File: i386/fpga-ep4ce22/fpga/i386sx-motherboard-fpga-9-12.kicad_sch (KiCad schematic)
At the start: 15 parts, among them J3 JTAG, J4 SPI ISP, J5 UART, U2 SN74AHCT1G125DBVR, U3 (3/6) EP4CE22F17C8N, U5 W25Q128JVSIQ

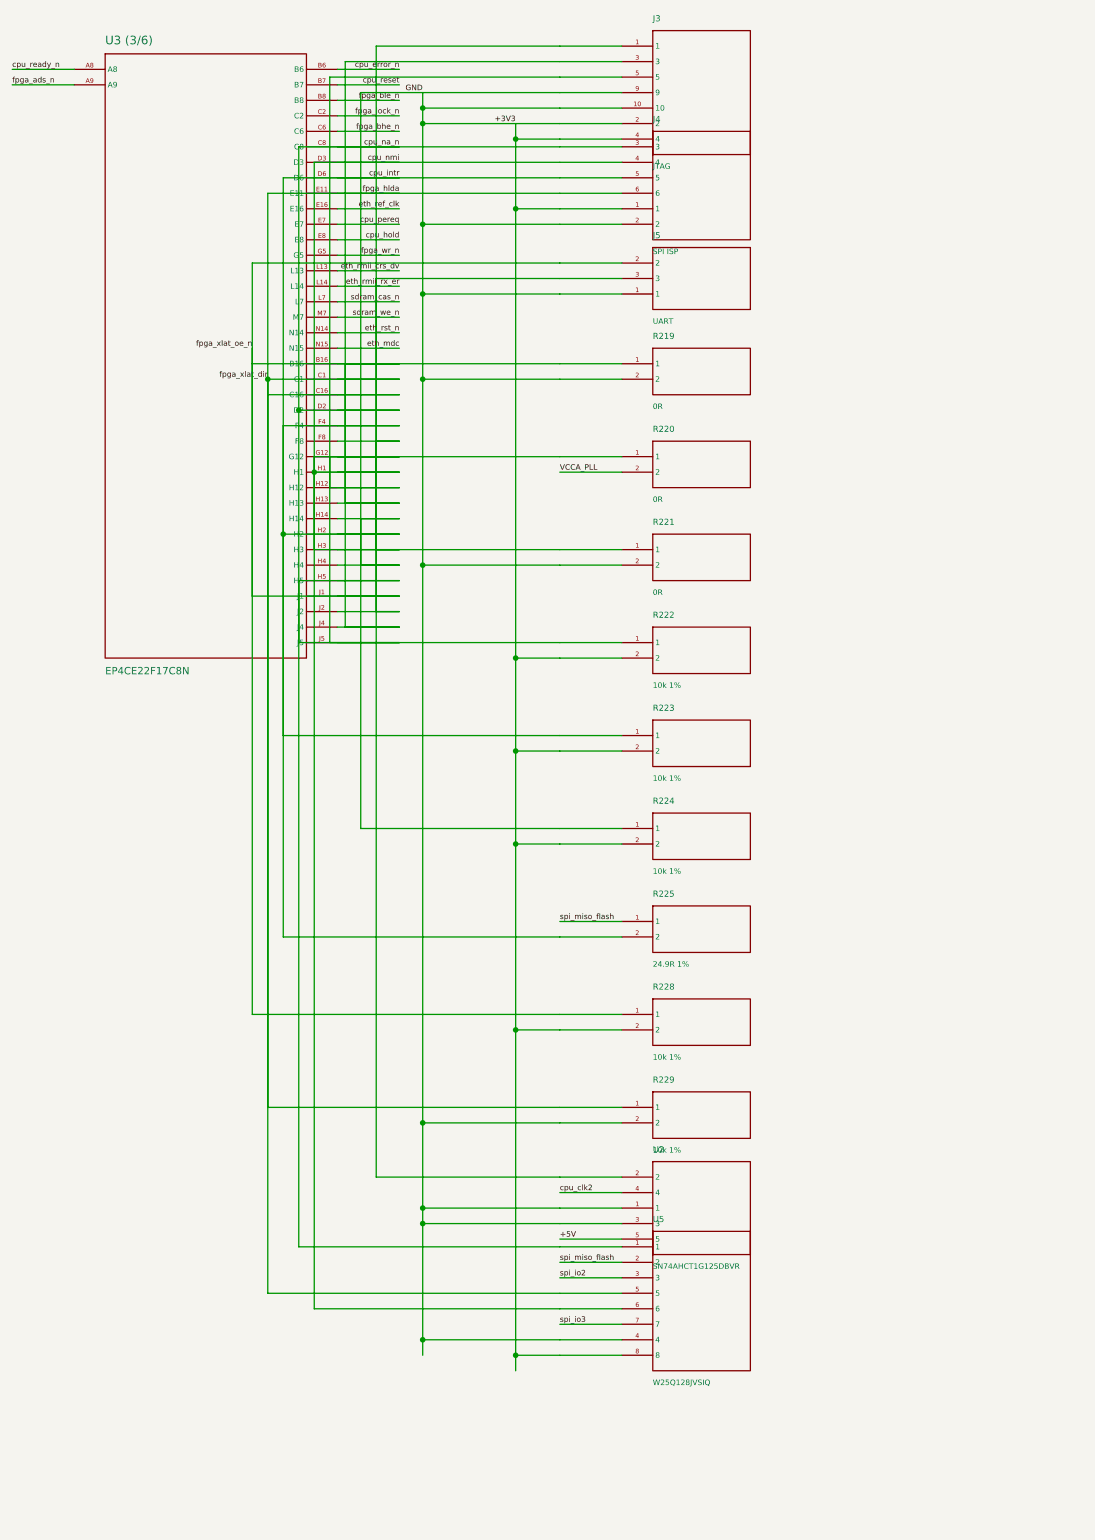
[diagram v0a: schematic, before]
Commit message: Publish the motherboards' KiCad files
From socket3@c0f6464 socket7@9205469 socket370@524f5b1 i386@bea926c
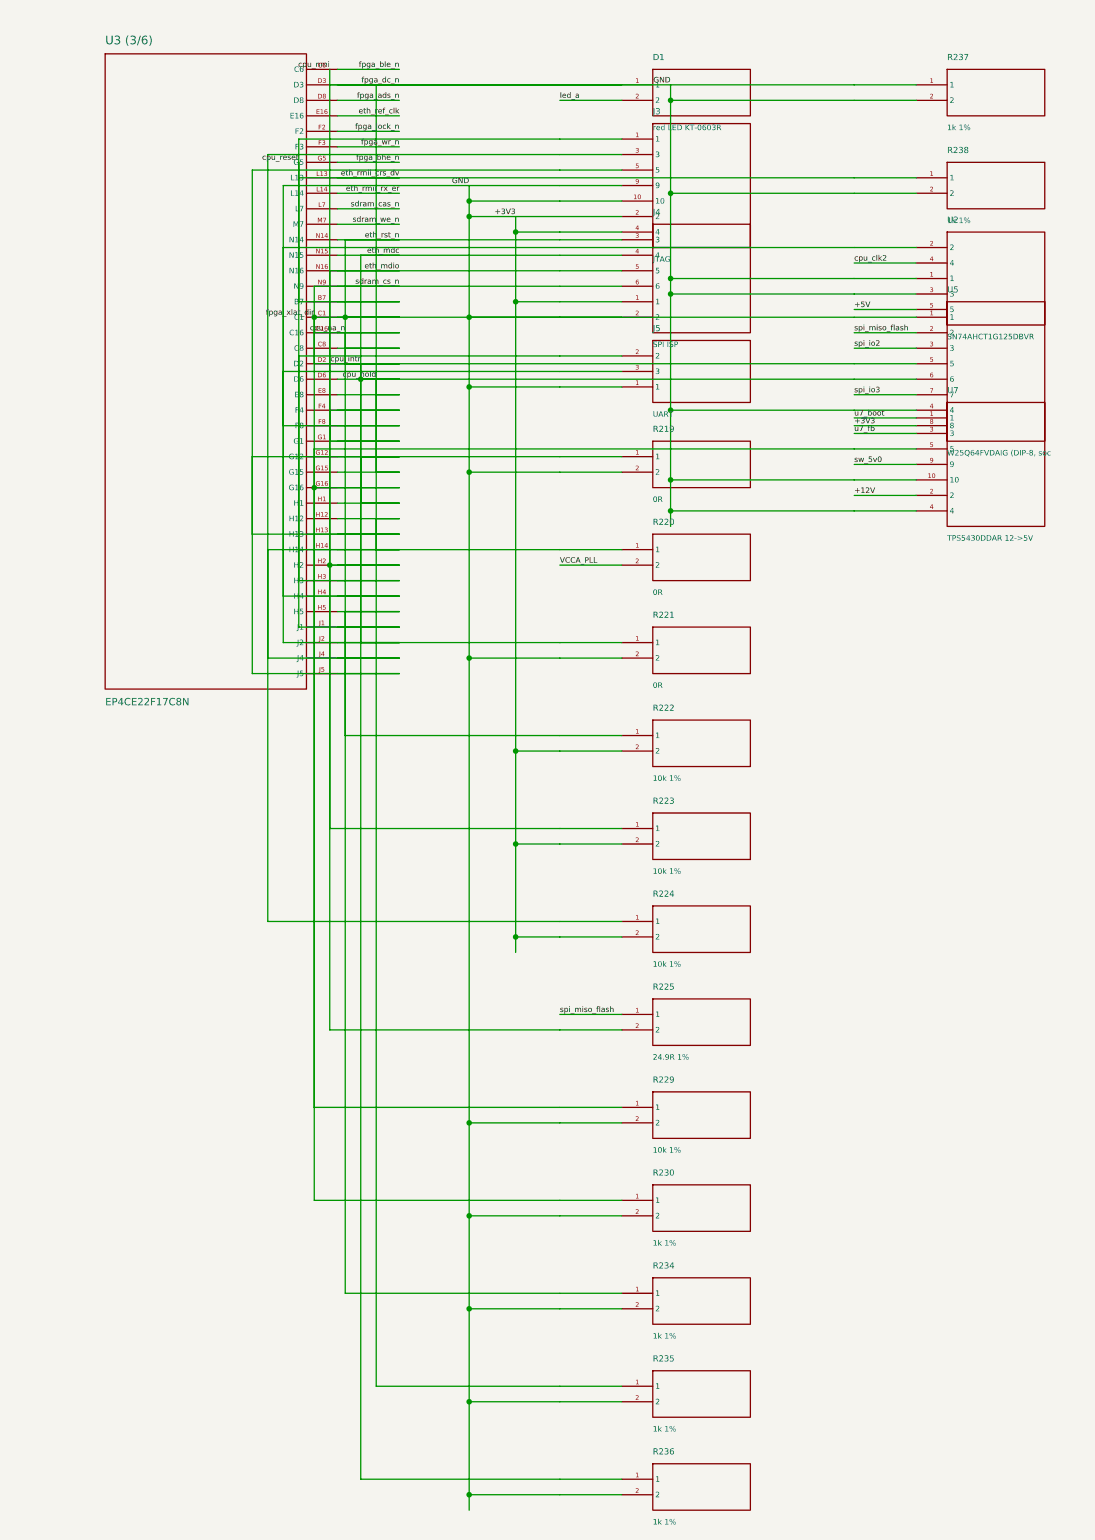
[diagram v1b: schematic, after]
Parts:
- removed R228: 10k 1%, symbol gen:S2_0s
- removed U3 (3/6): EP4CE22F17C8N, symbol gen:S2_38
- added D1: red LED KT-0603R, symbol gen:S2_0s
- added R230, R234, R235, R236, R237, R238: 1k 1%, symbol gen:S2_0s
- added U3 (3/6): EP4CE22F17C8N, symbol gen:S0_40
- added U7: TPS5430DDAR 12->5V, symbol gen:S7_0s
- U5: value W25Q128JVSIQ -> W25Q64FVDAIG (DIP-8, soc
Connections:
- net cpu_intr is gone; now on net +3V3: J4.5, R223.1, R225.2
- net fpga_hlda is gone; now on net +3V3: J4.6, R229.1, U5.5
- net +3V3: now also J3.3, J3.5, J4.3, J4.4, J5.3, R219.1, R220.1, R221.1, R222.1, U2.2, U5.1, U5.6, D1.1, R230.1, R230.2, R234.1, R234.2, R235.1, R235.2, R236.1, R236.2, R237.1, R237.2, R238.2, U3 (3/6).C1, U3 (3/6).C16, U3 (3/6).C8, U3 (3/6).D2, U3 (3/6).D3, U3 (3/6).D6, U3 (3/6).E8, U3 (3/6).F4, U3 (3/6).F8, U3 (3/6).G1, U3 (3/6).G12, U3 (3/6).G15, U3 (3/6).G16, U3 (3/6).H1, U3 (3/6).H12, U3 (3/6).H13, U3 (3/6).H14, U3 (3/6).H2, U3 (3/6).H4, U3 (3/6).H5, U3 (3/6).J2, U3 (3/6).J4, U3 (3/6).J5, U3 (3/6).N14, U3 (3/6).N15, U3 (3/6).N16, U3 (3/6).N9, U7.10, U7.4, U7.5
- net cpu_reset: now also J3.1, J5.2, R238.1, U3 (3/6).B7, U3 (3/6).H3, U3 (3/6).J1, U3 (3/6).L13
- net eth_ref_clk: now also U3 (3/6).E16
- net eth_rmii_rx_er: now also U3 (3/6).L14
- net fpga_ads_n: now also U3 (3/6).D8
- net fpga_bhe_n: now also U3 (3/6).G5
- net fpga_ble_n: now also U3 (3/6).C6
- net fpga_lock_n: now also U3 (3/6).F2
- net fpga_wr_n: now also U3 (3/6).F3
- net sdram_cas_n: now also U3 (3/6).L7
- net sdram_we_n: now also U3 (3/6).M7
- removed net cpu_na_n: J3.1, J3.5, J4.3, J4.4, J5.3, R220.1, R221.1, R222.1, U2.2, U5.1, U5.6
- removed net fpga_xlat_oe_n: J3.3, J5.2, R219.1
- new net +12V: U7.2
- new net led_a: D1.2
- new net sw_5v0: U7.9
- new net u7_boot: U7.1
- new net u7_fb: U7.3
